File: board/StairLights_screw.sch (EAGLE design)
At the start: 27 parts, among them J1 1,2, J2 3,4, J3 5,6, J4 7, 12V, J5 SIGN_TOP, J7 SIGN_BOTTOM, J8 SIGN_PWR, M1 ARDUINO-PRO-MINI-5.0VNOSIDEPI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

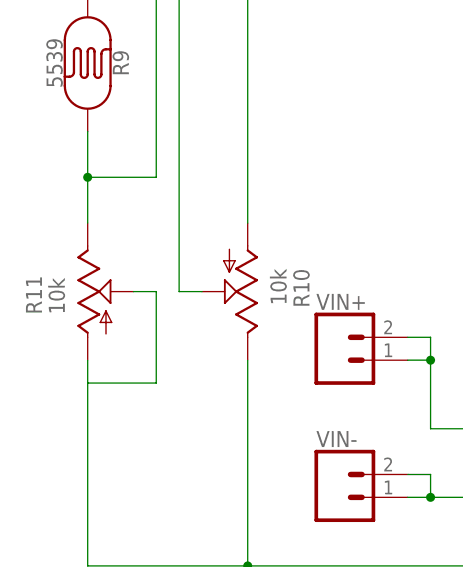
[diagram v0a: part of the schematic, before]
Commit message: Исправлена ошибка с номиналом потенциометра
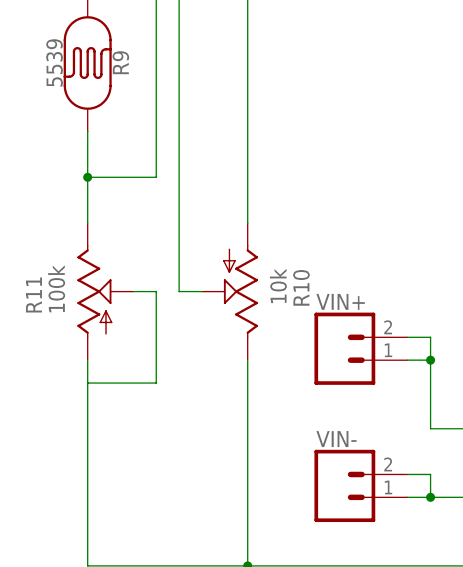
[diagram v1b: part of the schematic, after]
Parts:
- R11: value 10k -> 100k
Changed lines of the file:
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@@
 <part name="R8" library="SparkFun-Resistors" library_urn="urn:adsk.eagle:library:532" deviceset="330OHM" device="-HORIZ-1/10W-5%" package3d_urn="urn:adsk.eagle:package:39658/1" value="10k"/>
 <part name="R9" library="SparkFun-Sensors" deviceset="PHOTOCELL" device="PTH" value="5539"/>
-<part name="R11" library="pot" library_urn="urn:adsk.eagle:library:331" deviceset="TRIM_US-" device="S64W" package3d_urn="urn:adsk.eagle:package:22708/1" value="10k"/>
+<part name="R11" library="pot" library_urn="urn:adsk.eagle:library:331" deviceset="TRIM_US-" device="S64W" package3d_urn="urn:adsk.eagle:package:22708/1" value="100k"/>
 <part name="R10" library="pot" library_urn="urn:adsk.eagle:library:331" deviceset="TRIM_US-" device="S64W" package3d_urn="urn:adsk.eagle:package:22708/1" value="10k"/>
 </parts>
